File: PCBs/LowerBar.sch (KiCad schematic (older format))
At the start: 8 parts, among them J2 8 Pin Connector, SW1 SW_SPST, SW2 SW_SPST, SW3 SW_SPST, SW4 SW_SPST, SW5 SW_SPST, SW6 SW_SPST, SW7 SW_SPST

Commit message: Split up board, started routing traces
Moved the LED drivers and the STM32 board off of the main board and onto a daughterboard to fit a reasonable space. Second board will go behind the first, connected with .1" headers. 
Additionally, traces on the bottom four (second LED driver) OPT displays are routed. 
Redid the OPT buttons to be included in the keypad matrix, to save pins.
Removed the shift register pins and wired it all directly to the STM32, to save space
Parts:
- removed J2: 8 Pin Connector, UFC:8pin254mm, symbol Connector_Generic_MountingPin:Conn_01x08_MountingPin
- added D35, D36, D37, D38, D39, D40, D41: LED, LED_SMD:LED_0805_2012Metric_Pad1.15x1.40mm_HandSolder, symbol Device:LED
- added J2: 9pin, Connector_PinSocket_2.54mm:PinSocket_1x09_P2.54mm_Vertical, symbol Connector:Conn_01x09_Male
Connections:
- net labels added: LED, LEDPWM
- wire segments 34 -> 52
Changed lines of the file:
@@
 $Descr A4 11693 8268
 encoding utf-8
-Sheet 1 3
+Sheet 3 3
 Title ""
 Date ""
@@
 AR Path="/60A18B28" Ref="SW1"  Part="1"
 AR Path="/60A14FF3/60A18B28" Ref="SW18"  Part="1"
-F 0 "SW1" H 4850 3885 50  0000 C CNN
+F 0 "SW18" H 4850 3885 50  0000 C CNN
 F 1 "SW_SPST" H 4850 3794 50  0000 C CNN
 F 2 "Keypad:KailhSW" H 4850 3650 50  0001 C CNN
@@
 AR Path="/60A18B2E" Ref="SW2"  Part="1"
 AR Path="/60A14FF3/60A18B2E" Ref="SW19"  Part="1"
-F 0 "SW2" H 5300 3885 50  0000 C CNN
+F 0 "SW19" H 5300 3885 50  0000 C CNN
 F 1 "SW_SPST" H 5300 3794 50  0000 C CNN
 F 2 "Keypad:KailhSW" H 5300 3650 50  0001 C CNN
@@
 AR Path="/60A18B34" Ref="SW3"  Part="1"
 AR Path="/60A14FF3/60A18B34" Ref="SW20"  Part="1"
-F 0 "SW3" H 5750 3885 50  0000 C CNN
+F 0 "SW20" H 5750 3885 50  0000 C CNN
 F 1 "SW_SPST" H 5750 3794 50  0000 C CNN
 F 2 "Keypad:KailhSW" H 5750 3650 50  0001 C CNN
@@
 AR Path="/60A18B3A" Ref="SW4"  Part="1"
 AR Path="/60A14FF3/60A18B3A" Ref="SW21"  Part="1"
-F 0 "SW4" H 6200 3885 50  0000 C CNN
+F 0 "SW21" H 6200 3885 50  0000 C CNN
 F 1 "SW_SPST" H 6200 3794 50  0000 C CNN
 F 2 "Keypad:KailhSW" H 6200 3650 50  0001 C CNN
@@
 AR Path="/60A18B40" Ref="SW5"  Part="1"
 AR Path="/60A14FF3/60A18B40" Ref="SW22"  Part="1"
-F 0 "SW5" H 6650 3885 50  0000 C CNN
+F 0 "SW22" H 6650 3885 50  0000 C CNN
 F 1 "SW_SPST" H 6650 3794 50  0000 C CNN
 F 2 "Keypad:KailhSW" H 6650 3650 50  0001 C CNN
@@
 AR Path="/60A18B47" Ref="SW6"  Part="1"
 AR Path="/60A14FF3/60A18B47" Ref="SW23"  Part="1"
-F 0 "SW6" H 7100 3885 50  0000 C CNN
+F 0 "SW23" H 7100 3885 50  0000 C CNN
 F 1 "SW_SPST" H 7100 3794 50  0000 C CNN
 F 2 "Keypad:KailhSW" H 7100 3650 50  0001 C CNN
@@
 AR Path="/60A18B4D" Ref="SW7"  Part="1"
 AR Path="/60A14FF3/60A18B4D" Ref="SW24"  Part="1"
-F 0 "SW7" H 7550 3885 50  0000 C CNN
+F 0 "SW24" H 7550 3885 50  0000 C CNN
 F 1 "SW_SPST" H 7550 3794 50  0000 C CNN
 F 2 "Keypad:KailhSW" H 7550 3650 50  0001 C CNN
@@
 Text Label 4650 3450 0    50   ~ 0
 SW18
-$Comp
-L Connector_Generic_MountingPin:Conn_01x08_MountingPin J2
-U 1 1 60A19071
-P 2550 3550
-F 0 "J2" H 2637 3372 50  0000 L CNN
-F 1 "8 Pin Connector" H 2637 3463 50  0000 L CNN
-F 2 "UFC:8pin254mm" H 2550 3550 50  0001 C CNN
-F 3 "~" H 2550 3550 50  0001 C CNN
-	1    2550 3550
-	-1   0    0    1
-$EndComp
 Wire Wire Line
 	3550 3300 6200 3300
@@
 GND
 Wire Wire Line
-	2750 3850 4850 3850
+	2750 3850 3700 3850
 Wire Wire Line
 	2750 3750 3150 3750
@@
 Wire Wire Line
 	3850 3500 3850 3450
+$Comp
+L Device:LED D35
+U 1 1 60A25224
+P 3900 2450
+F 0 "D35" V 3939 2332 50  0000 R CNN
+F 1 "LED" V 3848 2332 50  0000 R CNN
+F 2 "LED_SMD:LED_0805_2012Metric_Pad1.15x1.40mm_HandSolder" H 3900 2450 50  0001 C CNN
+F 3 "~" H 3900 2450 50  0001 C CNN
+	1    3900 2450
+	0    -1   -1   0
+$EndComp
+$Comp
+L Device:LED D36
+U 1 1 60A26034
+P 4250 2450
+F 0 "D36" V 4289 2332 50  0000 R CNN
+F 1 "LED" V 4198 2332 50  0000 R CNN
+F 2 "LED_SMD:LED_0805_2012Metric_Pad1.15x1.40mm_HandSolder" H 4250 2450 50  0001 C CNN
+F 3 "~" H 4250 2450 50  0001 C CNN
+	1    4250 2450
+	0    -1   -1   0
+$EndComp
+$Comp
+L Device:LED D37
+U 1 1 60A268FA
+P 4600 2450
+F 0 "D37" V 4639 2332 50  0000 R CNN
+F 1 "LED" V 4548 2332 50  0000 R CNN
+F 2 "LED_SMD:LED_0805_2012Metric_Pad1.15x1.40mm_HandSolder" H 4600 2450 50  0001 C CNN
+F 3 "~" H 4600 2450 50  0001 C CNN
+	1    4600 2450
+	0    -1   -1   0
+$EndComp
+$Comp
+L Device:LED D38
+U 1 1 60A272DB
+P 4950 2450
+F 0 "D38" V 4989 2332 50  0000 R CNN
+F 1 "LED" V 4898 2332 50  0000 R CNN
+F 2 "LED_SMD:LED_0805_2012Metric_Pad1.15x1.40mm_HandSolder" H 4950 2450 50  0001 C CNN
+F 3 "~" H 4950 2450 50  0001 C CNN
+	1    4950 2450
+	0    -1   -1   0
+$EndComp
+$Comp
+L Device:LED D39
+U 1 1 60A27E76
+P 5300 2450
+F 0 "D39" V 5339 2332 50  0000 R CNN
+F 1 "LED" V 5248 2332 50  0000 R CNN
+F 2 "LED_SMD:LED_0805_2012Metric_Pad1.15x1.40mm_HandSolder" H 5300 2450 50  0001 C CNN
+F 3 "~" H 5300 2450 50  0001 C CNN
+	1    5300 2450
+	0    -1   -1   0
+$EndComp
+$Comp
+L Device:LED D40
+U 1 1 60A28917
+P 5650 2450
+F 0 "D40" V 5689 2332 50  0000 R CNN
+F 1 "LED" V 5598 2332 50  0000 R CNN
+F 2 "LED_SMD:LED_0805_2012Metric_Pad1.15x1.40mm_HandSolder" H 5650 2450 50  0001 C CNN
+F 3 "~" H 5650 2450 50  0001 C CNN
+	1    5650 2450
+	0    -1   -1   0
+$EndComp
+$Comp
+L Device:LED D41
+U 1 1 60A29133
+P 6000 2450
+F 0 "D41" V 6039 2332 50  0000 R CNN
+F 1 "LED" V 5948 2332 50  0000 R CNN
+F 2 "LED_SMD:LED_0805_2012Metric_Pad1.15x1.40mm_HandSolder" H 6000 2450 50  0001 C CNN
+F 3 "~" H 6000 2450 50  0001 C CNN
+	1    6000 2450
+	0    -1   -1   0
+$EndComp
+Wire Wire Line
+	6000 2300 5650 2300
+Connection ~ 3900 2300
+Connection ~ 4250 2300
+Wire Wire Line
+	4250 2300 3900 2300
+Connection ~ 4600 2300
+Wire Wire Line
+	4600 2300 4250 2300
+Connection ~ 4950 2300
+Wire Wire Line
+	4950 2300 4600 2300
+Connection ~ 5300 2300
+Wire Wire Line
+	5300 2300 4950 2300
+Connection ~ 5650 2300
+Wire Wire Line
+	5650 2300 5300 2300
+Wire Wire Line
+	6000 2600 5650 2600
+Connection ~ 3900 2600
+Connection ~ 4250 2600
+Wire Wire Line
+	4250 2600 3900 2600
+Connection ~ 4600 2600
+Wire Wire Line
+	4600 2600 4250 2600
+Connection ~ 4950 2600
+Wire Wire Line
+	4950 2600 4600 2600
+Connection ~ 5300 2600
+Wire Wire Line
+	5300 2600 4950 2600
+Connection ~ 5650 2600
+Wire Wire Line
+	5650 2600 5300 2600
+$Comp
+L Connector:Conn_01x09_Male J2
+U 1 1 60A2D5EF
+P 2550 3450
+F 0 "J2" H 2658 4031 50  0000 C CNN
+F 1 "9pin" H 2658 3940 50  0000 C CNN
+F 2 "Connector_PinSocket_2.54mm:PinSocket_1x09_P2.54mm_Vertical" H 2550 3450 50  0001 C CNN
+F 3 "~" H 2550 3450 50  0001 C CNN
+	1    2550 3450
+	1    0    0    -1
+$EndComp
+Wire Wire Line
+	3700 3850 3700 2600
+Wire Wire Line
+	3700 2600 3900 2600
+Connection ~ 3700 3850
+Wire Wire Line
+	3700 3850 4850 3850
+Wire Wire Line
+	3100 2300 3100 3050
+Wire Wire Line
+	3100 3050 2750 3050
+Wire Wire Line
+	3100 2300 3900 2300
+Text Label 3250 2300 0    50   ~ 0
+LEDPWM
+Text HLabel 3100 2800 0    50   Input ~ 0
+LED
 $EndSCHEMATC

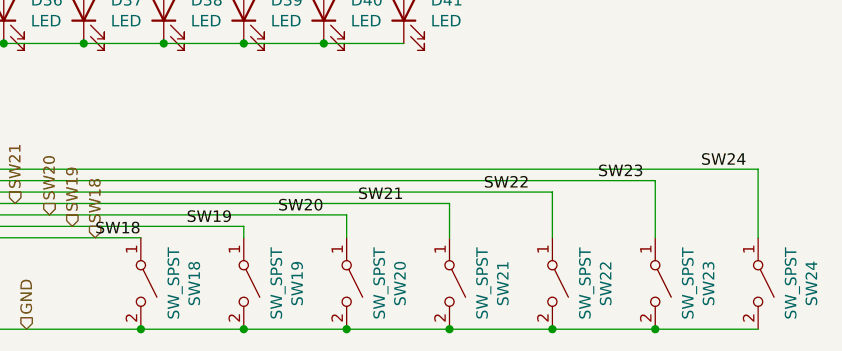
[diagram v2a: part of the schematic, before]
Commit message: Updated silkscreen, fixed minor issues
Updated silkscreen to include pin designations, and fixed minor issue with ground plane
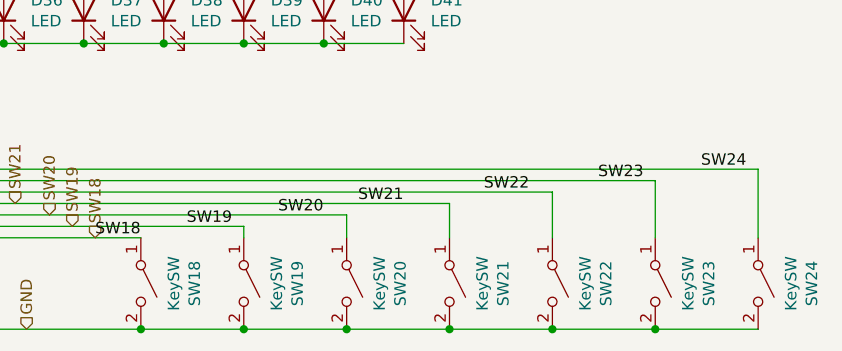
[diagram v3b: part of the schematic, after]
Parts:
- SW1, SW2, SW3, SW4, SW5, SW6, SW7: value SW_SPST -> KeySW
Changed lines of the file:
@@
 AR Path="/60A14FF3/60A18B28" Ref="SW18"  Part="1"
 F 0 "SW18" H 4850 3885 50  0000 C CNN
-F 1 "SW_SPST" H 4850 3794 50  0000 C CNN
+F 1 "KeySW" H 4850 3794 50  0000 C CNN
 F 2 "Keypad:KailhSW" H 4850 3650 50  0001 C CNN
 F 3 "~" H 4850 3650 50  0001 C CNN
@@
 AR Path="/60A14FF3/60A18B2E" Ref="SW19"  Part="1"
 F 0 "SW19" H 5300 3885 50  0000 C CNN
-F 1 "SW_SPST" H 5300 3794 50  0000 C CNN
+F 1 "KeySW" H 5300 3794 50  0000 C CNN
 F 2 "Keypad:KailhSW" H 5300 3650 50  0001 C CNN
 F 3 "~" H 5300 3650 50  0001 C CNN
@@
 AR Path="/60A14FF3/60A18B34" Ref="SW20"  Part="1"
 F 0 "SW20" H 5750 3885 50  0000 C CNN
-F 1 "SW_SPST" H 5750 3794 50  0000 C CNN
+F 1 "KeySW" H 5750 3794 50  0000 C CNN
 F 2 "Keypad:KailhSW" H 5750 3650 50  0001 C CNN
 F 3 "~" H 5750 3650 50  0001 C CNN
@@
 AR Path="/60A14FF3/60A18B3A" Ref="SW21"  Part="1"
 F 0 "SW21" H 6200 3885 50  0000 C CNN
-F 1 "SW_SPST" H 6200 3794 50  0000 C CNN
+F 1 "KeySW" H 6200 3794 50  0000 C CNN
 F 2 "Keypad:KailhSW" H 6200 3650 50  0001 C CNN
 F 3 "~" H 6200 3650 50  0001 C CNN
@@
 AR Path="/60A14FF3/60A18B40" Ref="SW22"  Part="1"
 F 0 "SW22" H 6650 3885 50  0000 C CNN
-F 1 "SW_SPST" H 6650 3794 50  0000 C CNN
+F 1 "KeySW" H 6650 3794 50  0000 C CNN
 F 2 "Keypad:KailhSW" H 6650 3650 50  0001 C CNN
 F 3 "~" H 6650 3650 50  0001 C CNN
@@
 AR Path="/60A14FF3/60A18B47" Ref="SW23"  Part="1"
 F 0 "SW23" H 7100 3885 50  0000 C CNN
-F 1 "SW_SPST" H 7100 3794 50  0000 C CNN
+F 1 "KeySW" H 7100 3794 50  0000 C CNN
 F 2 "Keypad:KailhSW" H 7100 3650 50  0001 C CNN
 F 3 "~" H 7100 3650 50  0001 C CNN
@@
 AR Path="/60A14FF3/60A18B4D" Ref="SW24"  Part="1"
 F 0 "SW24" H 7550 3885 50  0000 C CNN
-F 1 "SW_SPST" H 7550 3794 50  0000 C CNN
+F 1 "KeySW" H 7550 3794 50  0000 C CNN
 F 2 "Keypad:KailhSW" H 7550 3650 50  0001 C CNN
 F 3 "~" H 7550 3650 50  0001 C CNN

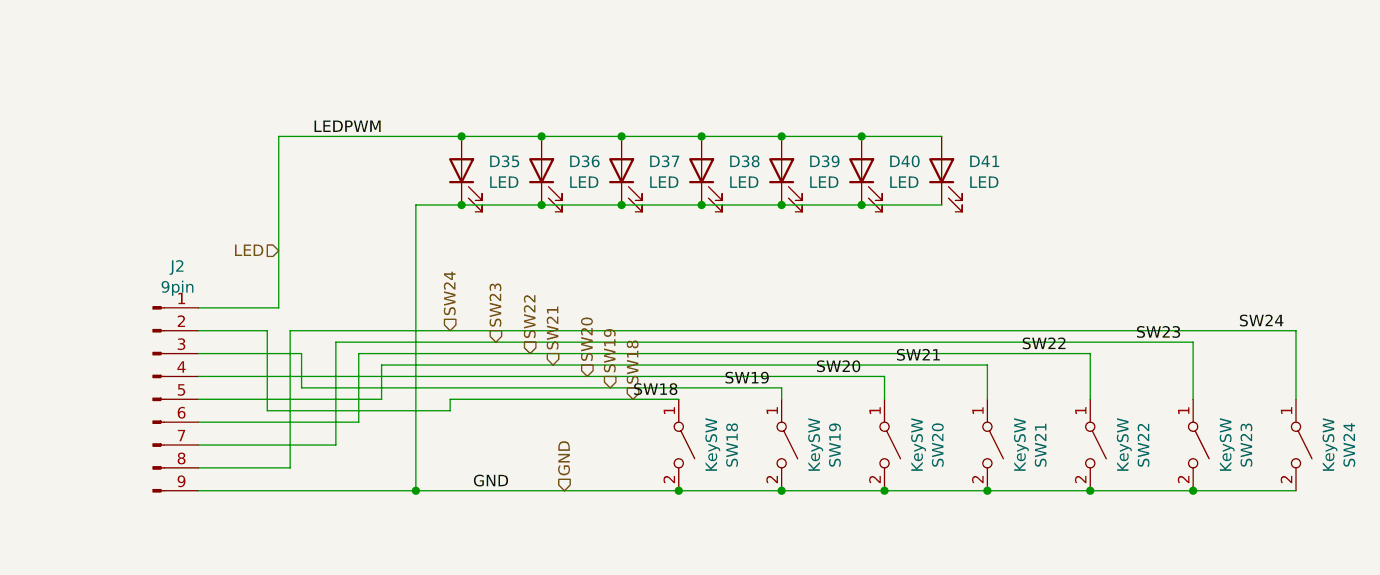
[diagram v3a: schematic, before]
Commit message: Fixed design error
Untested as of now.
Removed direct connection from PWM out to LEDs, as the PWM pins on the bluepill can't provide enough current. Added P channel mosfet, and individual resistors per parallel LED. For now, the single resistor for all LEDs is still present, but bypassable via jumper, for the sake of backwards compatibility.
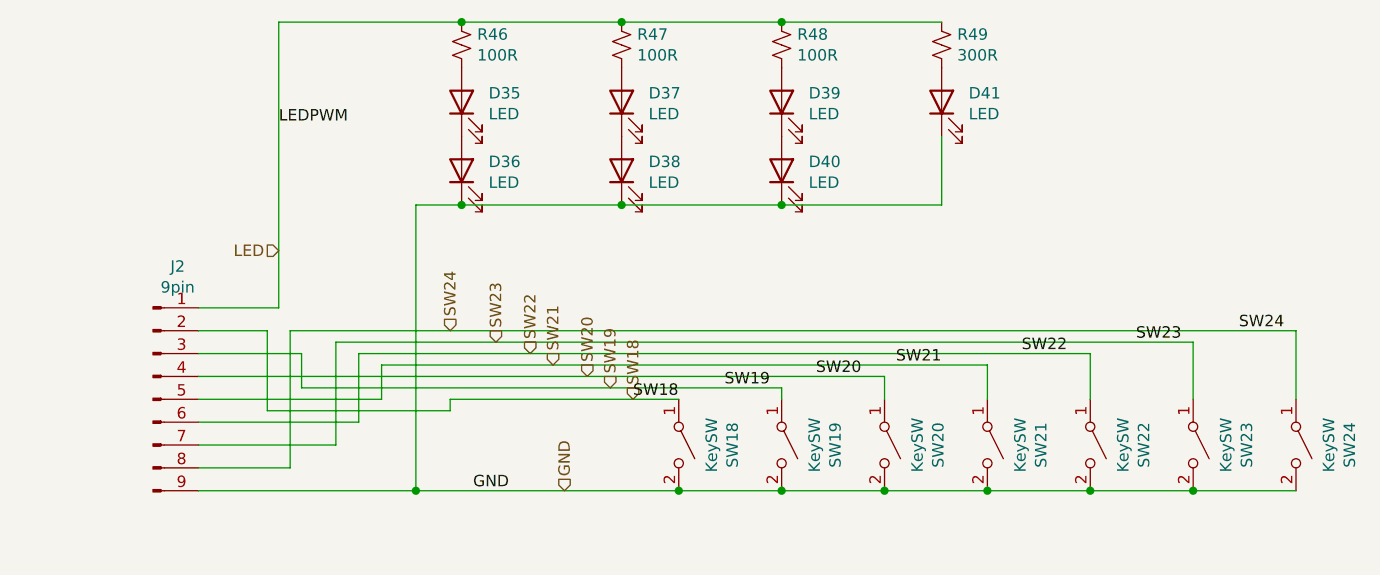
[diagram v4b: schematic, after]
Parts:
- added R46, R47, R48: 100R, Resistor_SMD:R_1206_3216Metric_Pad1.30x1.75mm_HandSolder, symbol Device:R_Small_US
- added R49: 300R, Resistor_SMD:R_1206_3216Metric_Pad1.30x1.75mm_HandSolder, symbol Device:R_Small_US
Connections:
- net GND: no longer D35.1 (K), D37.1 (K), D39.1 (K)
- net LED: now also R46.1, R47.1, R48.1, R49.1; no longer D35.2 (A), D36.2 (A), D37.2 (A), D38.2 (A), D39.2 (A), D40.2 (A), D41.2 (A)
- new net: D35.1 (K), D36.2 (A)
- new net: D35.2 (A), R46.2
- new net: D37.1 (K), D38.2 (A)
- new net: D37.2 (A), R47.2
- new net: D39.1 (K), D40.2 (A)
- new net: D39.2 (A), R48.2
- new net: D41.2 (A), R49.2
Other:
- moved on the sheet: D35, D36, D37, D38, D39, D40, D41
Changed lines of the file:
@@
 L Device:LED D35
 U 1 1 60A25224
+P 3900 2150
+F 0 "D35" V 3939 2032 50  0000 R CNN
+F 1 "LED" V 3848 2032 50  0000 R CNN
+F 2 "LED_SMD:LED_0805_2012Metric_Pad1.15x1.40mm_HandSolder" H 3900 2150 50  0001 C CNN
+F 3 "~" H 3900 2150 50  0001 C CNN
+	1    3900 2150
+	0    -1   -1   0
+$EndComp
+$Comp
+L Device:LED D36
+U 1 1 60A26034
 P 3900 2450
-F 0 "D35" V 3939 2332 50  0000 R CNN
+F 0 "D36" V 3939 2332 50  0000 R CNN
 F 1 "LED" V 3848 2332 50  0000 R CNN
 F 2 "LED_SMD:LED_0805_2012Metric_Pad1.15x1.40mm_HandSolder" H 3900 2450 50  0001 C CNN
@@
 $EndComp
 $Comp
-L Device:LED D36
-U 1 1 60A26034
-P 4250 2450
-F 0 "D36" V 4289 2332 50  0000 R CNN
-F 1 "LED" V 4198 2332 50  0000 R CNN
-F 2 "LED_SMD:LED_0805_2012Metric_Pad1.15x1.40mm_HandSolder" H 4250 2450 50  0001 C CNN
-F 3 "~" H 4250 2450 50  0001 C CNN
-	1    4250 2450
+L Device:LED D37
+U 1 1 60A268FA
+P 4600 2150
+F 0 "D37" V 4639 2032 50  0000 R CNN
+F 1 "LED" V 4548 2032 50  0000 R CNN
+F 2 "LED_SMD:LED_0805_2012Metric_Pad1.15x1.40mm_HandSolder" H 4600 2150 50  0001 C CNN
+F 3 "~" H 4600 2150 50  0001 C CNN
+	1    4600 2150
 	0    -1   -1   0
 $EndComp
 $Comp
-L Device:LED D37
-U 1 1 60A268FA
+L Device:LED D38
+U 1 1 60A272DB
 P 4600 2450
-F 0 "D37" V 4639 2332 50  0000 R CNN
+F 0 "D38" V 4639 2332 50  0000 R CNN
 F 1 "LED" V 4548 2332 50  0000 R CNN
 F 2 "LED_SMD:LED_0805_2012Metric_Pad1.15x1.40mm_HandSolder" H 4600 2450 50  0001 C CNN
@@
 $EndComp
 $Comp
-L Device:LED D38
-U 1 1 60A272DB
-P 4950 2450
-F 0 "D38" V 4989 2332 50  0000 R CNN
-F 1 "LED" V 4898 2332 50  0000 R CNN
-F 2 "LED_SMD:LED_0805_2012Metric_Pad1.15x1.40mm_HandSolder" H 4950 2450 50  0001 C CNN
-F 3 "~" H 4950 2450 50  0001 C CNN
-	1    4950 2450
+L Device:LED D39
+U 1 1 60A27E76
+P 5300 2150
+F 0 "D39" V 5339 2032 50  0000 R CNN
+F 1 "LED" V 5248 2032 50  0000 R CNN
+F 2 "LED_SMD:LED_0805_2012Metric_Pad1.15x1.40mm_HandSolder" H 5300 2150 50  0001 C CNN
+F 3 "~" H 5300 2150 50  0001 C CNN
+	1    5300 2150
 	0    -1   -1   0
 $EndComp
 $Comp
-L Device:LED D39
-U 1 1 60A27E76
+L Device:LED D40
+U 1 1 60A28917
 P 5300 2450
-F 0 "D39" V 5339 2332 50  0000 R CNN
+F 0 "D40" V 5339 2332 50  0000 R CNN
 F 1 "LED" V 5248 2332 50  0000 R CNN
 F 2 "LED_SMD:LED_0805_2012Metric_Pad1.15x1.40mm_HandSolder" H 5300 2450 50  0001 C CNN
@@
 $EndComp
 $Comp
-L Device:LED D40
-U 1 1 60A28917
-P 5650 2450
-F 0 "D40" V 5689 2332 50  0000 R CNN
-F 1 "LED" V 5598 2332 50  0000 R CNN
-F 2 "LED_SMD:LED_0805_2012Metric_Pad1.15x1.40mm_HandSolder" H 5650 2450 50  0001 C CNN
-F 3 "~" H 5650 2450 50  0001 C CNN
-	1    5650 2450
+L Device:LED D41
+U 1 1 60A29133
+P 6000 2150
+F 0 "D41" V 6039 2032 50  0000 R CNN
+F 1 "LED" V 5948 2032 50  0000 R CNN
+F 2 "LED_SMD:LED_0805_2012Metric_Pad1.15x1.40mm_HandSolder" H 6000 2150 50  0001 C CNN
+F 3 "~" H 6000 2150 50  0001 C CNN
+	1    6000 2150
 	0    -1   -1   0
 $EndComp
-$Comp
-L Device:LED D41
-U 1 1 60A29133
-P 6000 2450
-F 0 "D41" V 6039 2332 50  0000 R CNN
-F 1 "LED" V 5948 2332 50  0000 R CNN
-F 2 "LED_SMD:LED_0805_2012Metric_Pad1.15x1.40mm_HandSolder" H 6000 2450 50  0001 C CNN
-F 3 "~" H 6000 2450 50  0001 C CNN
-	1    6000 2450
-	0    -1   -1   0
-$EndComp
-Wire Wire Line
-	6000 2300 5650 2300
-Connection ~ 3900 2300
-Connection ~ 4250 2300
-Wire Wire Line
-	4250 2300 3900 2300
-Connection ~ 4600 2300
-Wire Wire Line
-	4600 2300 4250 2300
-Connection ~ 4950 2300
-Wire Wire Line
-	4950 2300 4600 2300
-Connection ~ 5300 2300
-Wire Wire Line
-	5300 2300 4950 2300
-Connection ~ 5650 2300
-Wire Wire Line
-	5650 2300 5300 2300
-Wire Wire Line
-	6000 2600 5650 2600
-Connection ~ 3900 2600
-Connection ~ 4250 2600
-Wire Wire Line
-	4250 2600 3900 2600
-Connection ~ 4600 2600
-Wire Wire Line
-	4600 2600 4250 2600
-Connection ~ 4950 2600
-Wire Wire Line
-	4950 2600 4600 2600
-Connection ~ 5300 2600
-Wire Wire Line
-	5300 2600 4950 2600
-Connection ~ 5650 2600
-Wire Wire Line
-	5650 2600 5300 2600
 $Comp
 L Connector:Conn_01x09_Male J2
@@
 Wire Wire Line
 	3700 3850 3700 2600
-Wire Wire Line
-	3700 2600 3900 2600
 Connection ~ 3700 3850
 Wire Wire Line
 	3700 3850 4850 3850
 Wire Wire Line
-	3100 2300 3100 3050
-Wire Wire Line
 	3100 3050 2750 3050
 Wire Wire Line
-	3100 2300 3900 2300
-Text Label 3250 2300 0    50   ~ 0
+	3100 1800 3900 1800
+Text Label 3100 2250 0    50   ~ 0
 LEDPWM
 Text HLabel 3100 2800 0    50   Input ~ 0
 LED
+$Comp
+L Device:R_Small_US R46
+U 1 1 60DFB409
+P 3900 1900
+F 0 "R46" H 3968 1946 50  0000 L CNN
+F 1 "100R" H 3968 1855 50  0000 L CNN
+F 2 "Resistor_SMD:R_1206_3216Metric_Pad1.30x1.75mm_HandSolder" H 3900 1900 50  0001 C CNN
+F 3 "~" H 3900 1900 50  0001 C CNN
+	1    3900 1900
+	1    0    0    -1
+$EndComp
+Wire Wire Line
+	3100 1800 3100 3050
+Wire Wire Line
+	3700 2600 3900 2600
+Connection ~ 3900 2600
+Wire Wire Line
+	3900 2600 4600 2600
+Connection ~ 4600 2600
+Wire Wire Line
+	4600 2600 5300 2600
+Wire Wire Line
+	5300 2600 6000 2600
+Wire Wire Line
+	6000 2600 6000 2300
+Connection ~ 5300 2600
+$Comp
+L Device:R_Small_US R47
+U 1 1 60E051B6
+P 4600 1900
+F 0 "R47" H 4668 1946 50  0000 L CNN
+F 1 "100R" H 4668 1855 50  0000 L CNN
+F 2 "Resistor_SMD:R_1206_3216Metric_Pad1.30x1.75mm_HandSolder" H 4600 1900 50  0001 C CNN
+F 3 "~" H 4600 1900 50  0001 C CNN
+	1    4600 1900
+	1    0    0    -1
+$EndComp
+$Comp
+L Device:R_Small_US R48
+U 1 1 60E06021
+P 5300 1900
+F 0 "R48" H 5368 1946 50  0000 L CNN
+F 1 "100R" H 5368 1855 50  0000 L CNN
+F 2 "Resistor_SMD:R_1206_3216Metric_Pad1.30x1.75mm_HandSolder" H 5300 1900 50  0001 C CNN
+F 3 "~" H 5300 1900 50  0001 C CNN
+	1    5300 1900
+	1    0    0    -1
+$EndComp
+$Comp
+L Device:R_Small_US R49
+U 1 1 60E06CCE
+P 6000 1900
+F 0 "R49" H 6068 1946 50  0000 L CNN
+F 1 "300R" H 6068 1855 50  0000 L CNN
+F 2 "Resistor_SMD:R_1206_3216Metric_Pad1.30x1.75mm_HandSolder" H 6000 1900 50  0001 C CNN
+F 3 "~" H 6000 1900 50  0001 C CNN
+	1    6000 1900
+	1    0    0    -1
+$EndComp
+Wire Wire Line
+	3900 1800 4600 1800
+Connection ~ 3900 1800
+Connection ~ 4600 1800
+Wire Wire Line
+	4600 1800 5300 1800
+Connection ~ 5300 1800
+Wire Wire Line
+	5300 1800 6000 1800
 $EndSCHEMATC
